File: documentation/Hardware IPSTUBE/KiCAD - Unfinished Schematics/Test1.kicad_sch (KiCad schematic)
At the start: 65 parts, among them J1 Conn_Coaxial_Small, P1 USB_C_Plug, Q1 Q_PNP_BCE, SW1 Reset Switch, U1 CH340N, U2 ESP32-PICO-D4, U4 DS1302Z+, U5 AT25SF081-SSHD-X, U6 MI6118, X1 Crystal, X3 Crystal

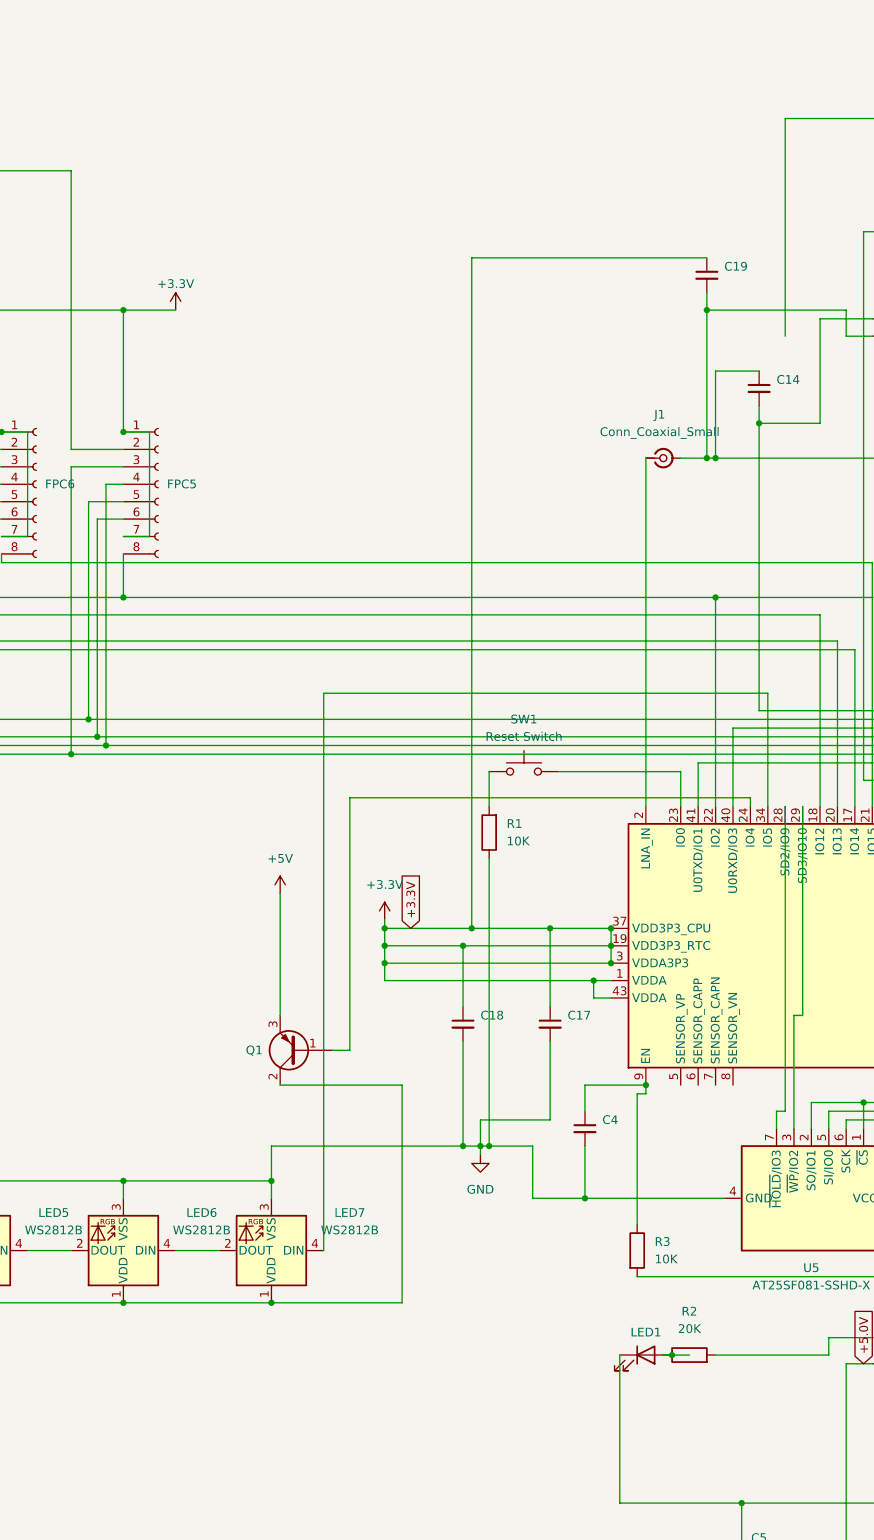
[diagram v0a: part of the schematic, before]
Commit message: Updated Schematics with Q1 logic
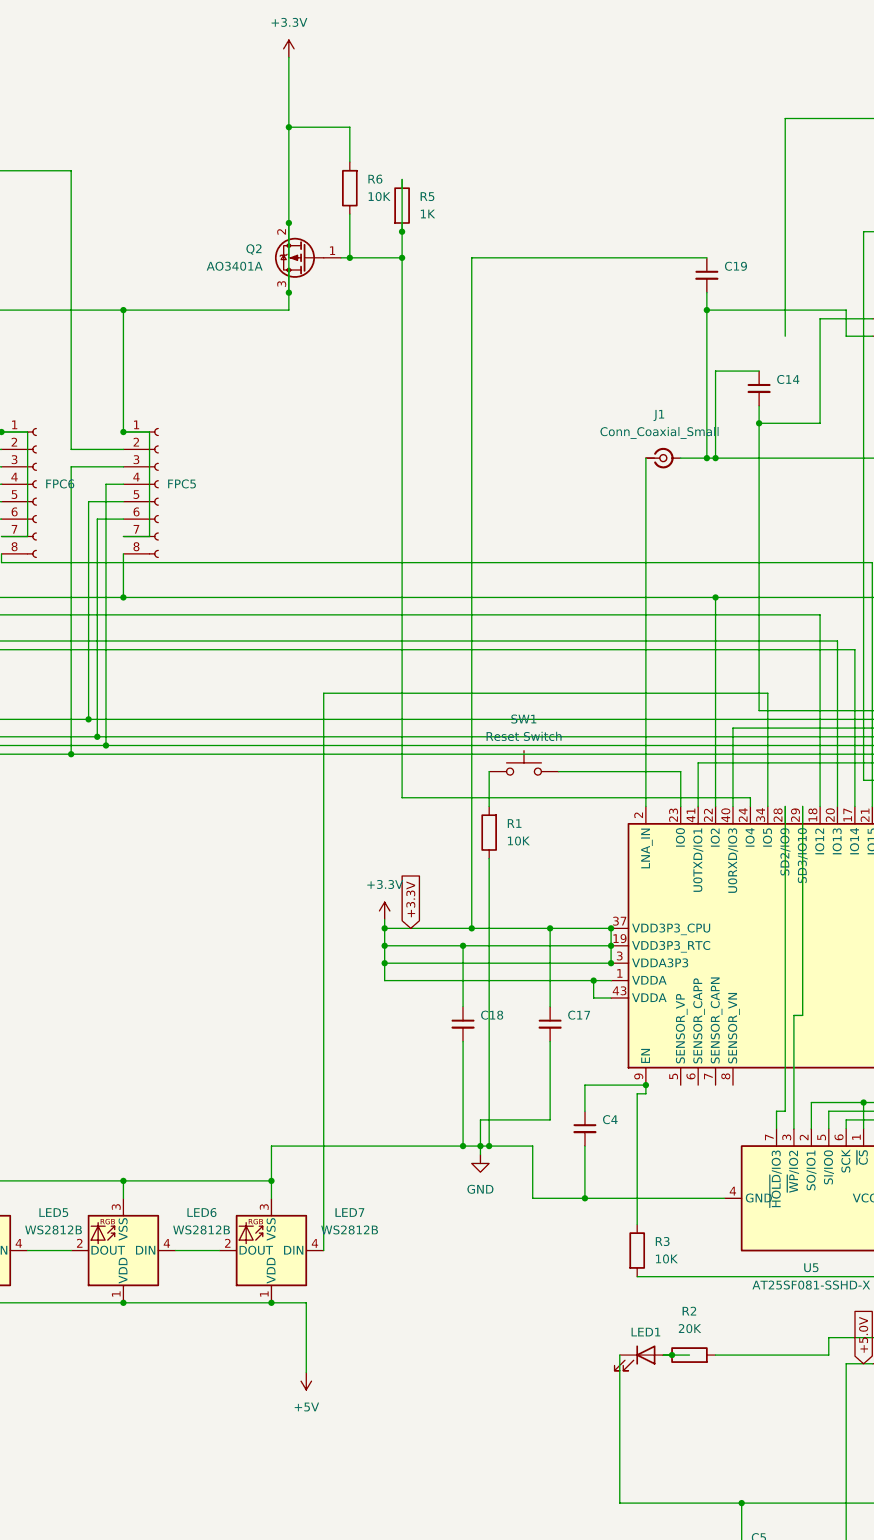
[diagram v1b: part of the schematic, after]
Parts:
- removed Q1: Q_PNP_BCE, symbol Device:Q_PNP_BCE
- added Q2: AO3401A, Package_TO_SOT_SMD:SOT-23, symbol Transistor_FET:AO3401A
- added R5: 1K, symbol Device:R
- added R6: 10K, symbol Device:R
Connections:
- net +3.3V: now also Q2.2 (S), Q2.3 (D), R6.2
- net +5V: now also LED2.1 (VDD), LED3.1 (VDD), LED4.1 (VDD), LED5.1 (VDD), LED6.1 (VDD), LED7.1 (VDD)
- net at U2.24 (IO4): now also Q2.1 (G), R5.1, R5.2, R6.1
